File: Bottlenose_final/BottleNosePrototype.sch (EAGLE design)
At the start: 22 parts, among them U1 MCP73831, X2 USBSMD

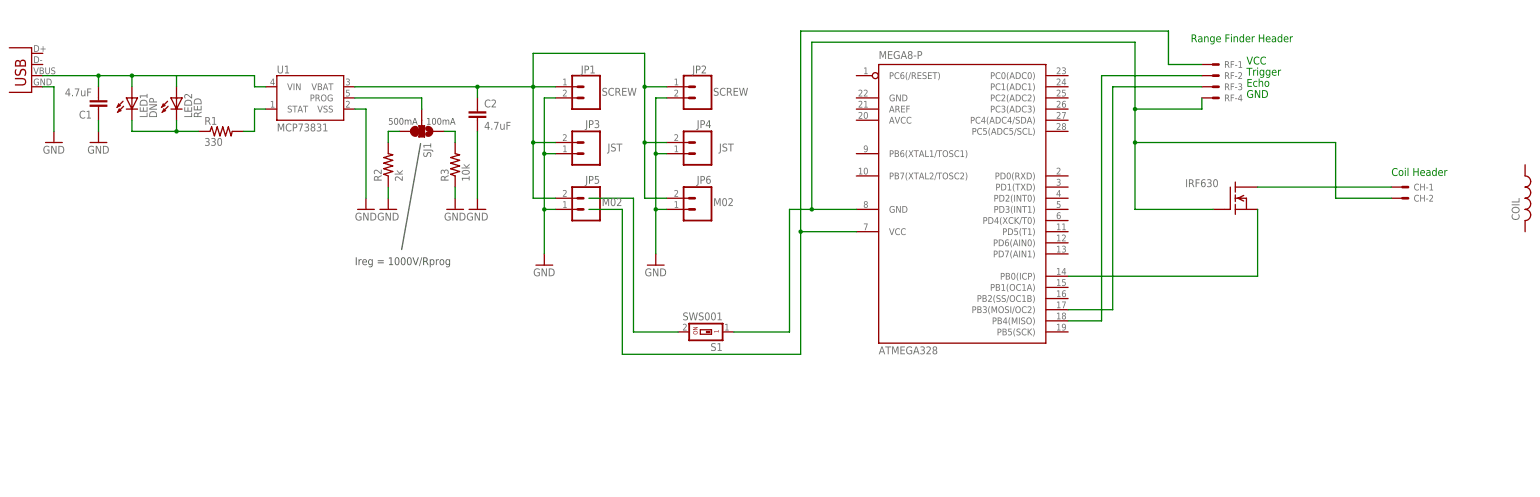
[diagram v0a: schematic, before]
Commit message: I have modified the Bottlenose_final/BottleNosePrototype.sch to add FTDI header and add crystal filter, the charging circuit was modified for our needs.
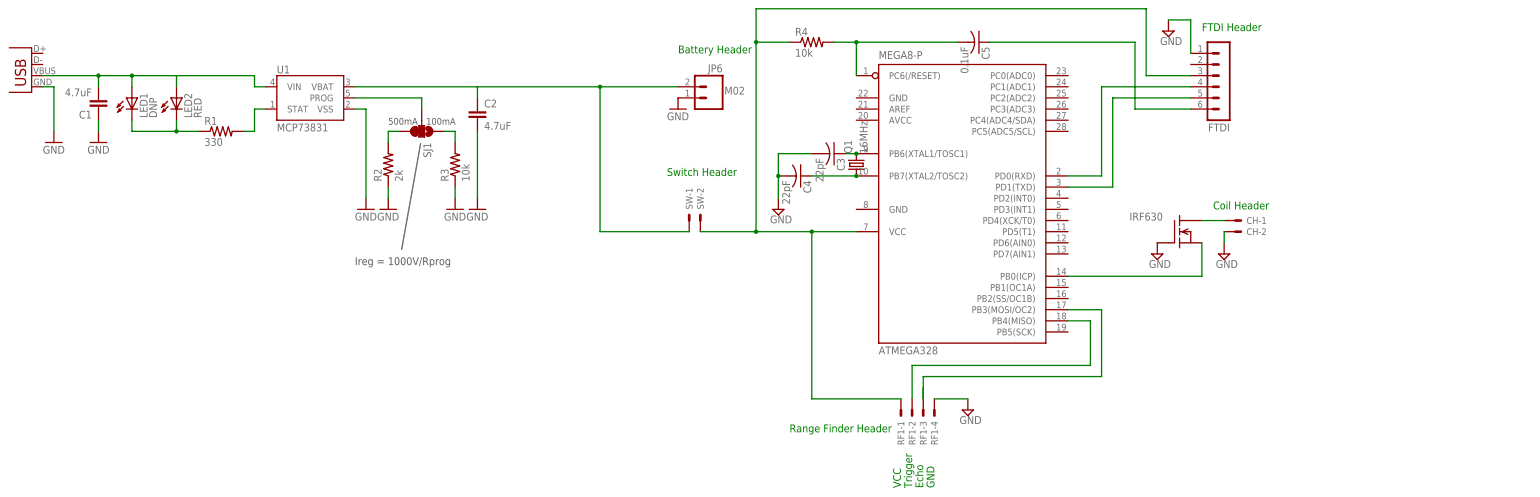
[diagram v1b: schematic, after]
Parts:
- removed COIL: (no value), rcl:L-US0204/7
- removed JP1, JP2: SCREW, SparkFun:M023.5MM-NO_SILK
- removed JP3, JP4: JST, SparkFun:M02JST-PTH-2
- removed JP5: M02, SparkFun:M02PTH
- removed RF: 22-23-2041, con-molex:22-23-2041
- removed S1: SWS001, smd-special:SWS001
- added C3, C4: 22pF, rcl:C-US025-024X044
- added C5: 0.1uF, rcl:C-US025-024X044
- added FTDI: (no value), con-lstb:MA06-1
- added Q1: 16MHz, crystal:CRYSTALTC26V
- added R4: 10k, resistor:R-US_0204/5
- added RF1: 22-23-2041, con-molex:22-23-2041
- added SW: 22-23-2021, con-molex:22-23-2021
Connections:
- removed net VBAT: C2.1, JP1.1, JP2.1, JP3.2, JP4.2, JP5.2, JP6.2, U1.VBAT
- new net N$12: ATMEGA328.PB7(XTAL2/TOSC2), C4.1, Q1.1
- new net N$13: ATMEGA328.PB3(MOSI/OC2), RF1-3.S
- new net N$15: ATMEGA328.PD1(TXD), FTDI.5
- new net N$17: C5.1, FTDI.6
- new net N$18: ATMEGA328.PC6(/RESET), C5.2, R4.2
- net GND: now also C3.2, C4.2, CH-2.S, FTDI.1, IRF630.G, RF1-4.S; no longer JP1.2, JP2.2, JP3.1, JP4.1, JP5.1
- net N$14: now also ATMEGA328.PD0(RXD), FTDI.4; no longer S1.2
- net N$5: now also ATMEGA328.VCC@1, FTDI.3, R4.1, RF1-1.S, SW-2.S; no longer ATMEGA328.GND@1, CH-2.S, IRF630.G, RF-4.S, S1.1
- net N$6: now also C2.1, JP6.2, SW-1.S, U1.VBAT; no longer ATMEGA328.VCC@1, RF-1.S
- net N$8: now also ATMEGA328.PB6(XTAL1/TOSC1), C3.1, Q1.2; no longer ATMEGA328.PB3(MOSI/OC2), RF-3.S
- net N$9: now also RF1-2.S; no longer RF-2.S
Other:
- note added: "Battery Header"
- note added: "FTDI Header"
- note added: "Switch Header"
- moved on the sheet: CH-1, CH-2, IRF630, JP6

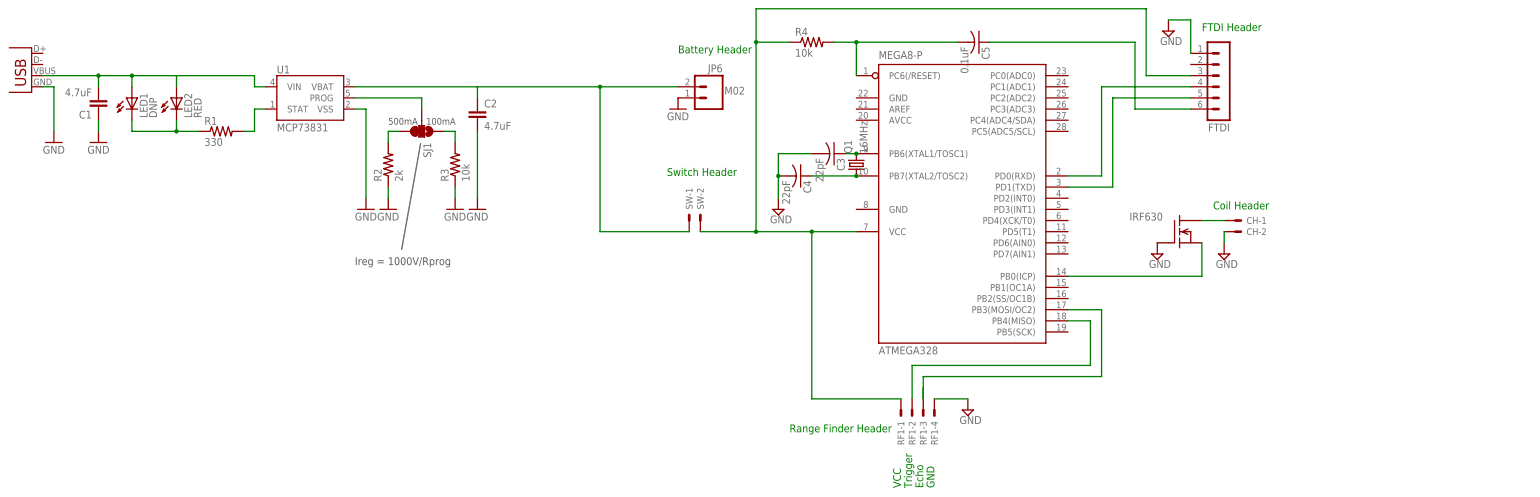
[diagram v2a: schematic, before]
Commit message: There was a couple of value errors
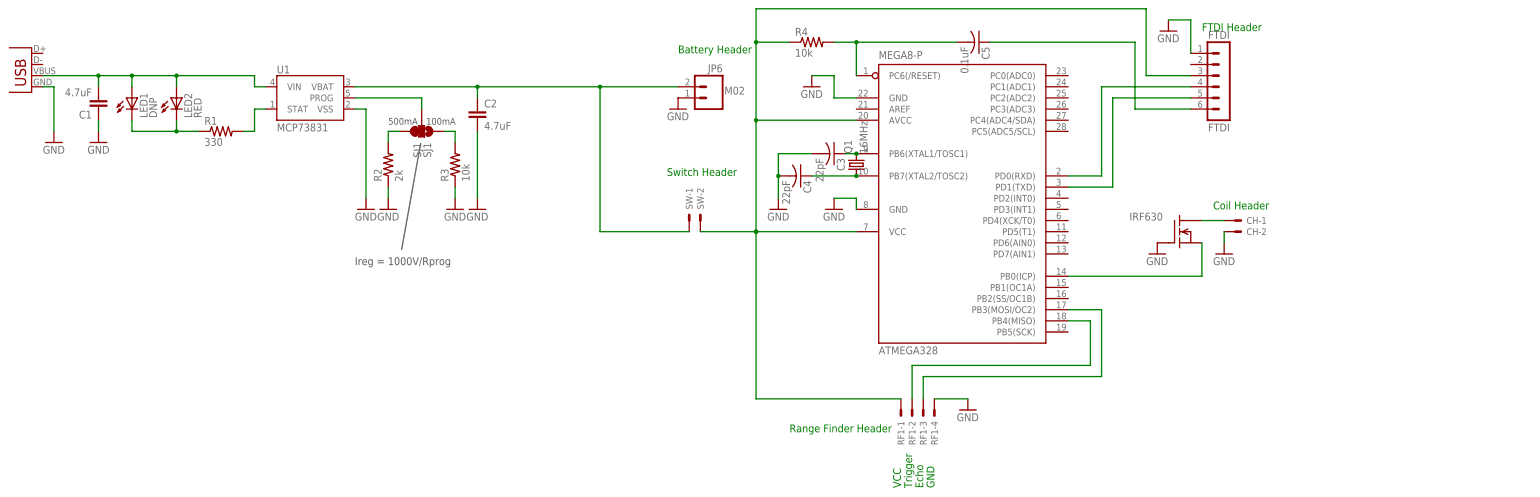
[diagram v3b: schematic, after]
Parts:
- FTDI: value (none) -> FTDI
- SJ1: value (none) -> SJ1
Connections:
- net GND: now also ATMEGA328.GND, ATMEGA328.GND@1
- net N$5: now also ATMEGA328.AVCC
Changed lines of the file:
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@@
 <part name="R2" library="SparkFun" deviceset="RESISTOR" device="0402-RES" value="2k"/>
 <part name="GND5" library="SparkFun" deviceset="GND" device=""/>
-<part name="SJ1" library="SparkFun" deviceset="SOLDERJUMPER_2WAY" device="S"/>
+<part name="SJ1" library="SparkFun" deviceset="SOLDERJUMPER_2WAY" device="S" value="SJ1"/>
 <part name="R3" library="SparkFun" deviceset="RESISTOR" device="0402-RES" value="10k"/>
 <part name="GND6" library="SparkFun" deviceset="GND" device=""/>
@@
 <part name="GND8" library="SparkFun" deviceset="GND" device=""/>
 <part name="CH" library="con-molex" deviceset="22-23-2021" device="" value=""/>
-<part name="SUPPLY1" library="supply2" deviceset="GND" device=""/>
-<part name="SUPPLY3" library="supply2" deviceset="GND" device=""/>
 <part name="RF1" library="con-molex" deviceset="22-23-2041" device="" value=""/>
-<part name="SUPPLY4" library="supply2" deviceset="GND" device=""/>
 <part name="SW" library="con-molex" deviceset="22-23-2021" device="" value=""/>
 <part name="Q1" library="crystal" deviceset="CRYSTAL" device="TC26V" value="16MHz"/>
 <part name="C3" library="rcl" deviceset="C-US" device="025-024X044" value="22pF"/>
 <part name="C4" library="rcl" deviceset="C-US" device="025-024X044" value="22pF"/>
-<part name="SUPPLY2" library="supply2" deviceset="GND" device=""/>
-<part name="FTDI" library="con-lstb" deviceset="MA06-1" device=""/>
-<part name="SUPPLY5" library="supply2" deviceset="GND" device=""/>
+<part name="FTDI" library="con-lstb" deviceset="MA06-1" device="" value="FTDI"/>
 <part name="R4" library="resistor" deviceset="R-US_" device="0204/5" value="10k"/>
 <part name="C5" library="rcl" deviceset="C-US" device="025-024X044" value="0.1uF"/>
+<part name="GND7" library="SparkFun" deviceset="GND" device=""/>
+<part name="GND9" library="SparkFun" deviceset="GND" device=""/>
+<part name="GND10" library="SparkFun" deviceset="GND" device=""/>
+<part name="GND11" library="SparkFun" deviceset="GND" device=""/>
+<part name="GND12" library="SparkFun" deviceset="GND" device=""/>
+<part name="GND13" library="SparkFun" deviceset="GND" device=""/>
+<part name="GND14" library="SparkFun" deviceset="GND" device=""/>
 </parts>
 <sheets>
@@
 <instance part="CH" gate="-1" x="139.7" y="38.1"/>
 <instance part="CH" gate="-2" x="139.7" y="35.56"/>
-<instance part="SUPPLY1" gate="GND" x="137.16" y="30.48"/>
-<instance part="SUPPLY3" gate="GND" x="121.92" y="30.48"/>
 <instance part="RF1" gate="-1" x="63.5" y="-5.08" rot="R270"/>
 <instance part="RF1" gate="-2" x="66.04" y="-5.08" rot="R270"/>
 <instance part="RF1" gate="-3" x="68.58" y="-5.08" rot="R270"/>
 <instance part="RF1" gate="-4" x="71.12" y="-5.08" rot="R270"/>
-<instance part="SUPPLY4" gate="GND" x="78.74" y="-5.08"/>
 <instance part="SW" gate="-1" x="15.24" y="38.1" rot="R90"/>
 <instance part="SW" gate="-2" x="17.78" y="38.1" rot="R90"/>
@@
 <instance part="C3" gate="G$1" x="48.26" y="53.34" rot="R270"/>
 <instance part="C4" gate="G$1" x="40.64" y="48.26" rot="R270"/>
-<instance part="SUPPLY2" gate="GND" x="35.56" y="40.64"/>
 <instance part="FTDI" gate="1" x="137.16" y="68.58" rot="R180"/>
-<instance part="SUPPLY5" gate="GND" x="124.46" y="81.28"/>
 <instance part="R4" gate="G$1" x="43.18" y="78.74"/>
 <instance part="C5" gate="G$1" x="81.28" y="78.74" rot="R270"/>
+<instance part="GND7" gate="1" x="121.92" y="30.48"/>
+<instance part="GND9" gate="1" x="78.74" y="-5.08"/>
+<instance part="GND10" gate="1" x="35.56" y="40.64"/>
+<instance part="GND11" gate="1" x="124.46" y="81.28"/>
+<instance part="GND12" gate="1" x="137.16" y="30.48"/>
+<instance part="GND13" gate="1" x="48.26" y="40.64"/>
+<instance part="GND14" gate="1" x="43.18" y="68.58"/>
 </instances>
 <busses>
@@
 <pinref part="LED1" gate="G$1" pin="A"/>
 <pinref part="U1" gate="G$1" pin="VIN"/>
+<junction x="-101.6" y="71.12"/>
 </segment>
 </net>
@@
 </segment>
 <segment>
-<pinref part="CH" gate="-2" pin="S"/>
-<pinref part="SUPPLY1" gate="GND" pin="GND"/>
-<wire x1="137.16" y1="33.02" x2="137.16" y2="35.56" width="0.1524" layer="91"/>
-</segment>
-<segment>
-<pinref part="IRF630" gate="G$1" pin="G"/>
-<pinref part="SUPPLY3" gate="GND" pin="GND"/>
-</segment>
-<segment>
-<pinref part="RF1" gate="-4" pin="S"/>
-<pinref part="SUPPLY4" gate="GND" pin="GND"/>
-<wire x1="71.12" y1="-2.54" x2="78.74" y2="-2.54" width="0.1524" layer="91"/>
+<pinref part="JP6" gate="G$1" pin="1"/>
+<pinref part="GND8" gate="1" pin="GND"/>
+</segment>
+<segment>
+<pinref part="ATMEGA328" gate="G$1" pin="GND"/>
+<wire x1="53.34" y1="66.04" x2="48.26" y2="66.04" width="0.1524" layer="91"/>
+<wire x1="48.26" y1="66.04" x2="48.26" y2="71.12" width="0.1524" layer="91"/>
+<wire x1="48.26" y1="71.12" x2="43.18" y2="71.12" width="0.1524" layer="91"/>
+<pinref part="GND14" gate="1" pin="GND"/>
+</segment>
+<segment>
+<wire x1="48.26" y1="43.18" x2="53.34" y2="43.18" width="0.1524" layer="91"/>
+<pinref part="ATMEGA328" gate="G$1" pin="GND@1"/>
+<wire x1="53.34" y1="43.18" x2="53.34" y2="40.64" width="0.1524" layer="91"/>
+<pinref part="GND13" gate="1" pin="GND"/>
 </segment>
 <segment>
 <pinref part="C3" gate="G$1" pin="2"/>
 <wire x1="43.18" y1="53.34" x2="35.56" y2="53.34" width="0.1524" layer="91"/>
-<pinref part="SUPPLY2" gate="GND" pin="GND"/>
 <wire x1="35.56" y1="53.34" x2="35.56" y2="48.26" width="0.1524" layer="91"/>
 <pinref part="C4" gate="G$1" pin="2"/>
 <junction x="35.56" y="48.26"/>
 <wire x1="35.56" y1="48.26" x2="35.56" y2="43.18" width="0.1524" layer="91"/>
-</segment>
-<segment>
-<pinref part="JP6" gate="G$1" pin="1"/>
-<pinref part="GND8" gate="1" pin="GND"/>
-</segment>
-<segment>
-<pinref part="SUPPLY5" gate="GND" pin="GND"/>
+<pinref part="GND10" gate="1" pin="GND"/>
+</segment>
+<segment>
+<pinref part="RF1" gate="-4" pin="S"/>
+<wire x1="71.12" y1="-2.54" x2="78.74" y2="-2.54" width="0.1524" layer="91"/>
+<pinref part="GND9" gate="1" pin="GND"/>
+</segment>
+<segment>
+<pinref part="IRF630" gate="G$1" pin="G"/>
+<pinref part="GND7" gate="1" pin="GND"/>
+</segment>
+<segment>
 <wire x1="124.46" y1="83.82" x2="129.54" y2="83.82" width="0.1524" layer="91"/>
 <pinref part="FTDI" gate="1" pin="1"/>
 <wire x1="129.54" y1="83.82" x2="129.54" y2="76.2" width="0.1524" layer="91"/>
+<pinref part="GND11" gate="1" pin="GND"/>
+</segment>
+<segment>
+<pinref part="CH" gate="-2" pin="S"/>
+<wire x1="137.16" y1="33.02" x2="137.16" y2="35.56" width="0.1524" layer="91"/>
+<pinref part="GND12" gate="1" pin="GND"/>
 </segment>
 </net>
@@
 </segment>
 </net>
-<net name="N$11" class="0">
-<segment>
-<pinref part="IRF630" gate="G$1" pin="D"/>
-<pinref part="CH" gate="-1" pin="S"/>
-<wire x1="132.08" y1="38.1" x2="137.16" y2="38.1" width="0.1524" layer="91"/>
-</segment>
-</net>
 <net name="N$13" class="0">
 <segment>
 <pinref part="RF1" gate="-3" pin="S"/>
-<wire x1="68.58" y1="-2.54" x2="68.58" y2="0" width="0.1524" layer="91"/>
 <wire x1="68.58" y1="-2.54" x2="68.58" y2="2.54" width="0.1524" layer="91"/>
 <wire x1="68.58" y1="2.54" x2="109.22" y2="2.54" width="0.1524" layer="91"/>
@@
 <segment>
 <pinref part="ATMEGA328" gate="G$1" pin="VCC@1"/>
-<wire x1="53.34" y1="35.56" x2="43.18" y2="35.56" width="0.1524" layer="91"/>
+<wire x1="53.34" y1="35.56" x2="30.48" y2="35.56" width="0.1524" layer="91"/>
 <pinref part="RF1" gate="-1" pin="S"/>
-<wire x1="63.5" y1="-2.54" x2="43.18" y2="-2.54" width="0.1524" layer="91"/>
-<wire x1="43.18" y1="-2.54" x2="43.18" y2="35.56" width="0.1524" layer="91"/>
+<wire x1="63.5" y1="-2.54" x2="30.48" y2="-2.54" width="0.1524" layer="91"/>
+<wire x1="30.48" y1="-2.54" x2="30.48" y2="35.56" width="0.1524" layer="91"/>
 <pinref part="SW" gate="-2" pin="S"/>
 <wire x1="17.78" y1="35.56" x2="30.48" y2="35.56" width="0.1524" layer="91"/>
-<junction x="43.18" y="35.56"/>
+<junction x="30.48" y="35.56"/>
 <pinref part="FTDI" gate="1" pin="3"/>
-<wire x1="30.48" y1="35.56" x2="43.18" y2="35.56" width="0.1524" layer="91"/>
 <wire x1="129.54" y1="71.12" x2="119.38" y2="71.12" width="0.1524" layer="91"/>
 <wire x1="119.38" y1="71.12" x2="119.38" y2="86.36" width="0.1524" layer="91"/>
@@
 <junction x="30.48" y="35.56"/>
 <pinref part="R4" gate="G$1" pin="1"/>
-<wire x1="30.48" y1="78.74" x2="30.48" y2="35.56" width="0.1524" layer="91"/>
+<wire x1="30.48" y1="78.74" x2="30.48" y2="60.96" width="0.1524" layer="91"/>
+<wire x1="30.48" y1="60.96" x2="30.48" y2="35.56" width="0.1524" layer="91"/>
 <wire x1="38.1" y1="78.74" x2="30.48" y2="78.74" width="0.1524" layer="91"/>
 <junction x="30.48" y="78.74"/>
+<pinref part="ATMEGA328" gate="G$1" pin="AVCC"/>
+<wire x1="53.34" y1="60.96" x2="30.48" y2="60.96" width="0.1524" layer="91"/>
+<junction x="30.48" y="60.96"/>
 </segment>
 </net>
@@
 <pinref part="JP6" gate="G$1" pin="2"/>
 <junction x="-5.08" y="68.58"/>
+<junction x="-33.02" y="68.58"/>
 </segment>
 </net>
@@
 </segment>
 </net>
+<net name="N$1" class="0">
+<segment>
+<pinref part="CH" gate="-1" pin="S"/>
+<pinref part="IRF630" gate="G$1" pin="D"/>
+<wire x1="137.16" y1="38.1" x2="132.08" y2="38.1" width="0.1524" layer="91"/>
+</segment>
+</net>
